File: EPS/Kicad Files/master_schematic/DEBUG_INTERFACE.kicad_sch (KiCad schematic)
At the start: 12 parts, among them J2 Generic_Conn_01x05

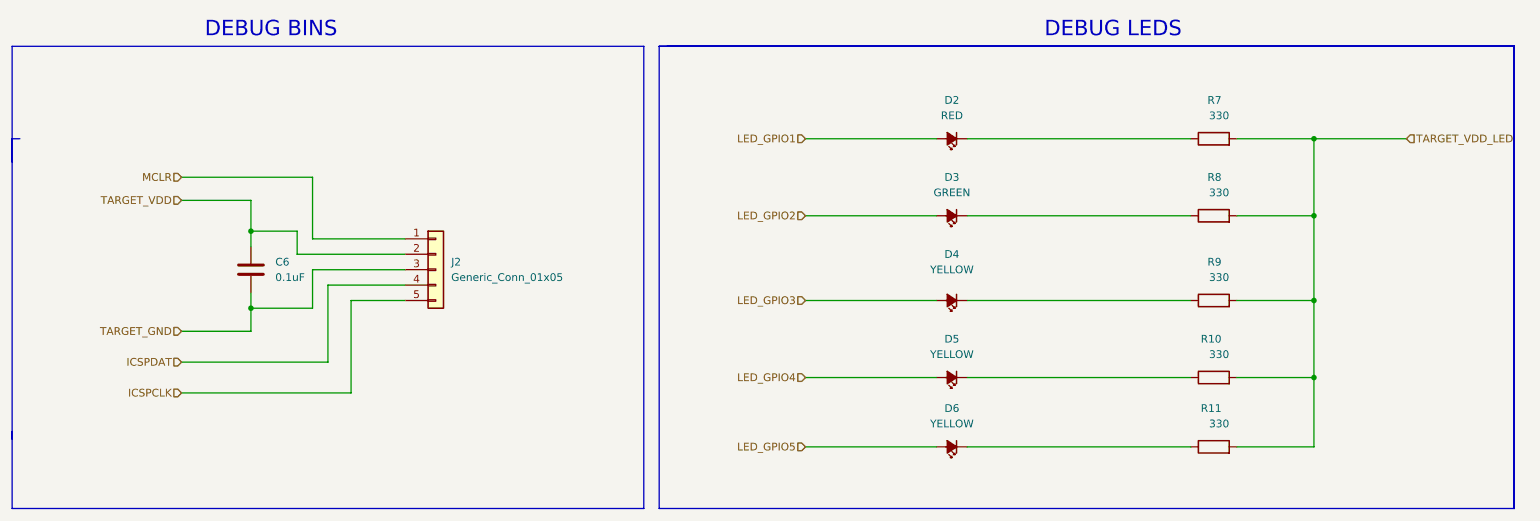
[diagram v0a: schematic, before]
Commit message: updated master schematic
should be nearing final schematic revision. run electrical rules check next
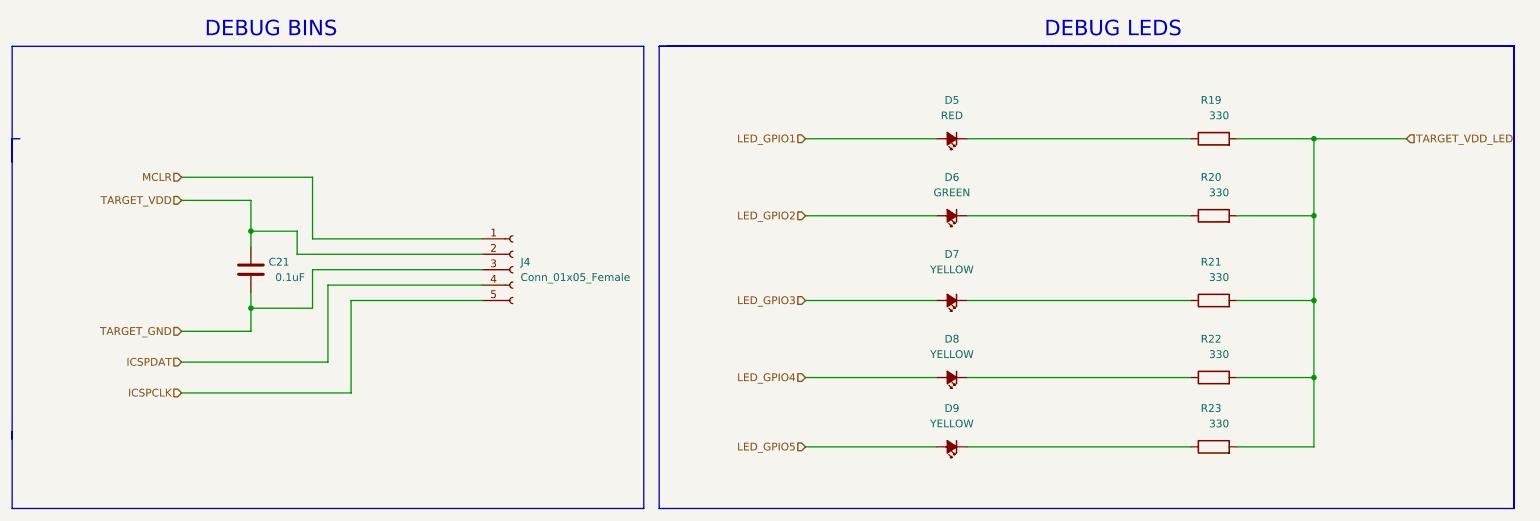
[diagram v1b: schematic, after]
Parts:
- removed J2: Generic_Conn_01x05, Connector_PinHeader_2.54mm:PinHeader_1x05_P2.54mm_Vertical, symbol avionics_board-cache:Connector_Generic_Conn_01x05
- added J4: Conn_01x05_Female, Connector_PinSocket_2.54mm:PinSocket_1x05_P2.54mm_Vertical, symbol Connector:Conn_01x05_Female
- C21: renamed from C6; footprint Capacitor_SMD:C_0603_1608Metric_Pad1.08x0.95mm_HandSolder -> Capacitor_SMD:C_0603_1608Metric
- D5: renamed from D2; footprint LED_SMD:LED_0603_1608Metric_Pad1.05x0.95mm_HandSolder -> LED_SMD:LED_0603_1608Metric
- D6: renamed from D3; footprint LED_SMD:LED_0603_1608Metric_Pad1.05x0.95mm_HandSolder -> LED_SMD:LED_0603_1608Metric
- D7: renamed from D4; footprint LED_SMD:LED_0603_1608Metric_Pad1.05x0.95mm_HandSolder -> LED_SMD:LED_0603_1608Metric
- D8: renamed from D5; footprint LED_SMD:LED_0603_1608Metric_Pad1.05x0.95mm_HandSolder -> LED_SMD:LED_0603_1608Metric
- D9: renamed from D6; footprint LED_SMD:LED_0603_1608Metric_Pad1.05x0.95mm_HandSolder -> LED_SMD:LED_0603_1608Metric
- R19: renamed from R7; footprint Resistor_SMD:R_0603_1608Metric_Pad0.98x0.95mm_HandSolder -> Resistor_SMD:R_0603_1608Metric
- R20: renamed from R8; footprint Resistor_SMD:R_0603_1608Metric_Pad0.98x0.95mm_HandSolder -> Resistor_SMD:R_0603_1608Metric
- R21: renamed from R9; footprint Resistor_SMD:R_0603_1608Metric_Pad0.98x0.95mm_HandSolder -> Resistor_SMD:R_0603_1608Metric
- R22: renamed from R10; footprint Resistor_SMD:R_0603_1608Metric_Pad0.98x0.95mm_HandSolder -> Resistor_SMD:R_0603_1608Metric
- R23: renamed from R11; footprint Resistor_SMD:R_0603_1608Metric_Pad0.98x0.95mm_HandSolder -> Resistor_SMD:R_0603_1608Metric
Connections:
- net ICSPCLK: now also J4.5 (Pin_5)
- net ICSPDAT: now also J4.4 (Pin_4)
- net MCLR: now also J4.1 (Pin_1)
- net TARGET_GND: now also J4.3 (Pin_3)
- net TARGET_VDD: now also J4.2 (Pin_2)
